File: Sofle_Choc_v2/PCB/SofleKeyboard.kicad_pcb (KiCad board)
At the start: 2 copper layers, 143.4 x 111.8 mm, 84 parts, among them J2 4PIN, J3 OLED, P1 i2c_pin, P2 i2c_pin, SW1 SW_PUSH_LED, SW10 SW_PUSH_LED, SW11 SW_PUSH_LED, SW12 SW_PUSH_LED, SW13 SW_PUSH_LED, SW14 SW_PUSH_LED, SW15 SW_PUSH_LED, SW16 SW_PUSH_LED, SW17 SW_PUSH_LED, SW18 SW_PUSH_LED, SW19 SW_PUSH_LED, SW2 SW_PUSH_LED, SW20 SW_PUSH_LED, SW21 SW_PUSH_LED, SW22 SW_PUSH_LED, SW23 SW_PUSH_LED, SW24 SW_PUSH_LED, SW25 Rotary_Encoder_Switch, SW26 SW_PUSH_LED, SW27 SW_PUSH_LED, SW28 SW_PUSH_LED, SW29 SW_PUSH_LED, SW3 SW_PUSH_LED, SW30 SW_PUSH_LED, SW4 SW_PUSH_LED, SW5 SW_PUSH_LED, SW6 SW_PUSH_LED, SW7 SW_PUSH_LED, SW8 SW_PUSH_LED, SW9 SW_PUSH_LED, U1 ProMicro

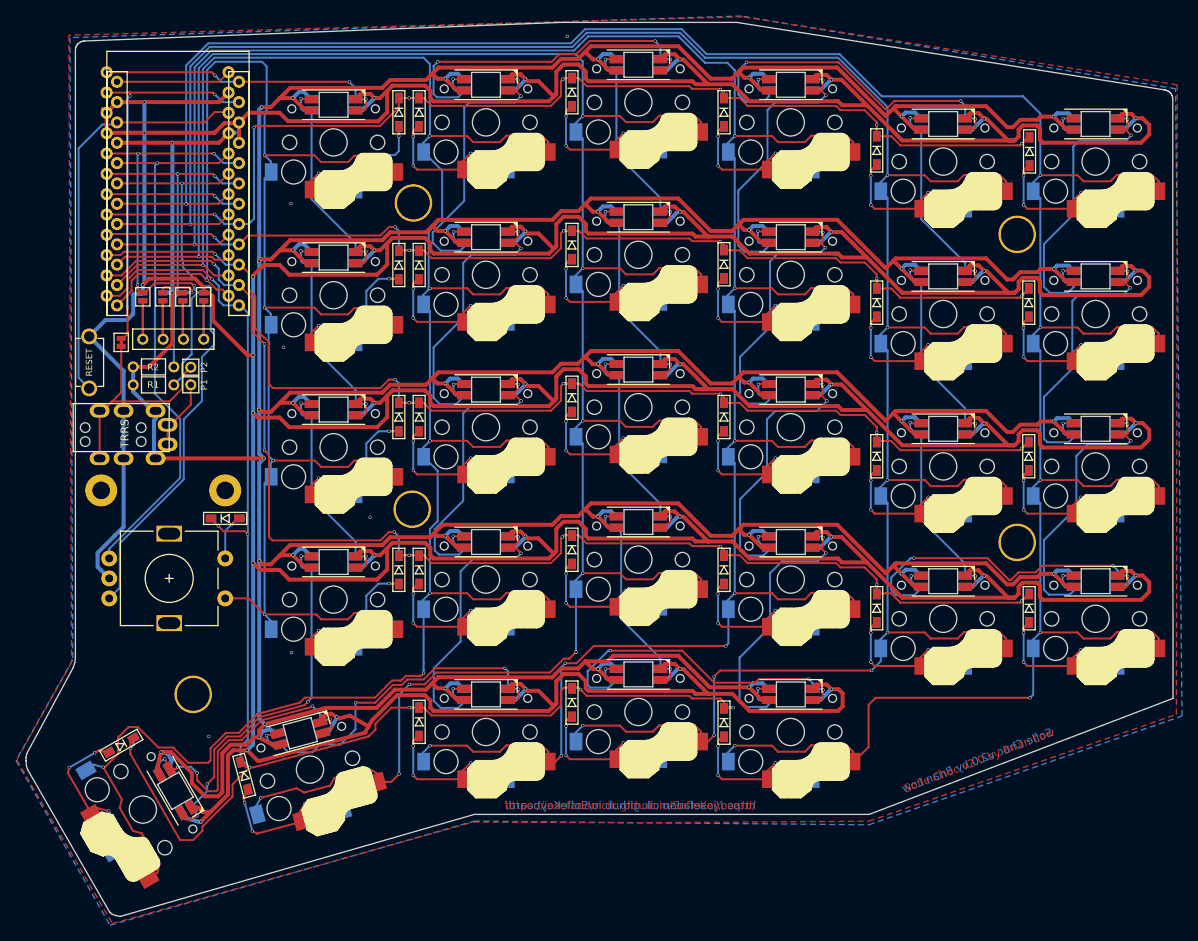
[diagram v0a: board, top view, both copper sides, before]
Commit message: Fix traces too close to pads
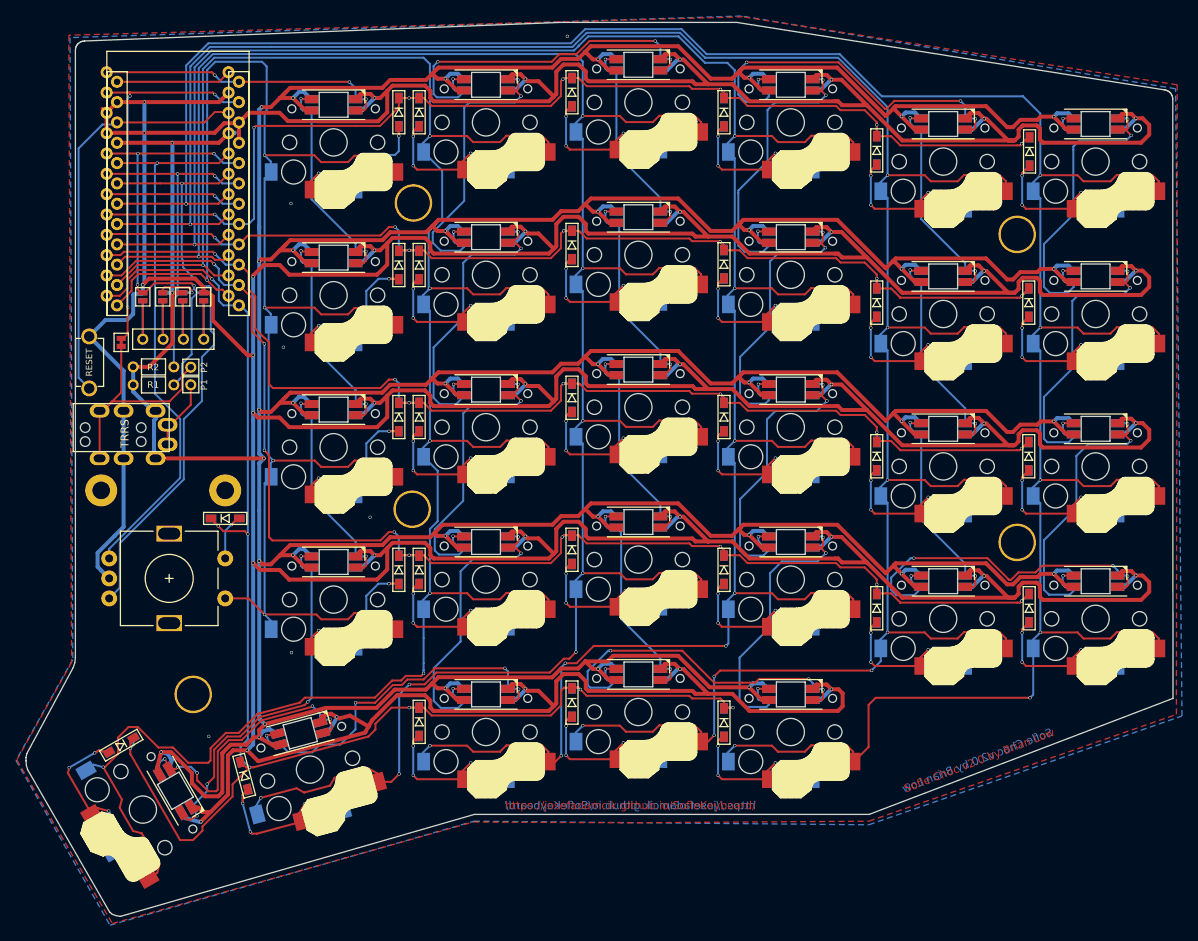
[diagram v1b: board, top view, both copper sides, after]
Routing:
- net Net-(D27-Pad2): track 22.6 -> 23.6 mm

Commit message: Bump to version 2.1
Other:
- board text added: "Sofle Choc v2.1 by Brian Low"
- board text removed: "Sofle Choc v2.0 by Brian Low"
